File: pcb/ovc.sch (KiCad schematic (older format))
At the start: 234 parts

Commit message: finished schematic and starting location of components, advance in analog front end
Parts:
- removed C? (x21): C, symbol Device:C
- removed J? (x5): Conn_01x04, symbol Connector_Generic:Conn_01x04
- removed J? (x5): Conn_01x02, symbol Connector_Generic:Conn_01x02
- removed J?: Conn_02x03_Counter_Clockwise, symbol Connector_Generic:Conn_02x03_Counter_Clockwise
- removed R? (x2): R, VC:VC-RES-0603-1608metric, symbol Device:R
- removed R? (x2): 5k, VC:VC-RES-0603-1608metric, symbol Device:R
- removed R? (x6): 10k, VC:VC-RES-0603-1608metric, symbol Device:R
- added C14, C19, C2, C22, C24, C27, C28, C30, C32, C40, C41, C59, C6, C60, C62, C63, C70, C71, C73, C74, C80, C86: 100nF, VC:murata-CAP-GCM-0603-1608metric-reflow, symbol Device:C
- added C53, C78: 470uF, Capacitor_SMD:C_Elec_10x10.2, symbol Device:CP
- added C67, C79, C84, C85: 10uF, VC:murata-CAP-GRM-0805-2012metric-reflow, symbol Device:C
- added D12, D14: SM6T39CA, VC:ST-DO214AA, symbol vc_misc:SM6T39CA
- added D27: LTST-C191KRKT, digikey-footprints:LED_0603, symbol dk_LED-Indication-Discrete:LTST-C191KRKT
- added J1: Conn_01x12, VC:phoenix_contact-therminal_block-12pos_PTSA1.5_12-3.5-F-1985069, symbol Connector_Generic:Conn_01x12
- added J10, J11, J7, J8: Conn_01x04, Connector_Molex:Molex_Nano-Fit_105309-xx04_1x04_P2.50mm_Vertical, symbol Connector_Generic:Conn_01x04
- added J13: Conn_02x11_Odd_Even, Connector_PinHeader_2.54mm:PinHeader_2x11_P2.54mm_Vertical_SMD, symbol Connector_Generic:Conn_02x11_Odd_Even
- added J16: Conn_01x31, VC:Omron-XF2M-3015-1A, symbol Connector_Generic:Conn_01x31
- added J21, J22: Conn_01x08, Connector_PinHeader_2.54mm:PinHeader_1x08_P2.54mm_Vertical, symbol Connector_Generic:Conn_01x08
- added J23: Conn_01x10, Connector_FFC-FPC:Hirose_FH12-10S-0.5SH_1x10-1MP_P0.50mm_Horizontal, symbol Connector_Generic:Conn_01x10
- added J3: Conn_02x04_Counter_Clockwise, VC:VC-SOICbite-vcpinout, symbol Connector_Generic:Conn_02x04_Counter_Clockwise
- added J4: Conn_01x04, Connector_Phoenix_MSTB:PhoenixContact_MSTBA_2,5_4-G_1x04_P5.00mm_Horizontal, symbol Connector_Generic:Conn_01x04
- added J9: Conn_01x02, Connector_Phoenix_MSTB:PhoenixContact_MSTBA_2,5_2-G_1x02_P5.00mm_Horizontal, symbol Connector_Generic:Conn_01x02
- added Q10, Q11, Q12, Q8, Q9: MMBT3906, Package_TO_SOT_SMD:SOT-23, symbol Transistor_BJT:MMBT3906
- added R2, R4: 4.99k, VC:VC-RES-0603-1608metric, symbol Device:R
- added R29, R30: 10r, VC:VC-RES-0603-1608metric, symbol Device:R
- added R35, R36, R37: 5K1, VC:VC-RES-0603-1608metric, symbol Device:R
- added R63, R67, R75, R78, R81: 1k, VC:VC-RES-0603-1608metric, symbol Device:R
- added R69, R70, R71, R89, R90: 10k, VC:VC-RES-0603-1608metric, symbol Device:R
- added R83, R84, R85, R88, R91, R92, R93, R94, R95: 330, VC:VC-RES-0603-1608metric, symbol Device:R
- added U13, U15: SN74HC595N, digikey-footprints:DIP-16_W7.62mm, symbol dk_Logic-Shift-Registers:SN74HC595N
- added U7: SN74LVC3G17, VC:TexasInstruments_DCU8_R-PDSO-G8_0.5mm, symbol vc_misc:SN74LVC3G17
- C1, C11, C12, C16, C17, C18, C20, C21, C3, C31, C33, C34, C37, C38, C39, C43, C44, C46, C47, C48, C5, C56, C58, C7, C76, C81: renamed from C?; footprint (none) -> VC:murata-CAP-GCM-0603-1608metric-reflow
- C10, C50, C52, C68: renamed from C?; value C -> 100nF; footprint (none) -> VC:murata-CAP-GCM-0603-1608metric-reflow
- C13, C35, C36, C4, C45, C55, C57, C66, C83, C9: renamed from C?; footprint (none) -> VC:murata-CAP-GRM-0805-2012metric-reflow
- C42, C51, C61, C64, C69, C72, C75: renamed from C?; value CP -> 47uF; footprint (none) -> Capacitor_SMD:C_Elec_6.3x5.8
- C54: renamed from C?; value CP -> 470uF; footprint (none) -> Capacitor_SMD:C_Elec_10x10.2
- J12: renamed from J?; footprint (none) -> Connector_PinHeader_2.54mm:PinHeader_2x10_P2.54mm_Vertical_SMD
- J14, J15: renamed from J?; footprint (none) -> Connector_PinHeader_2.54mm:PinHeader_1x04_P2.54mm_Vertical
- J18: renamed from J?; footprint (none) -> Connector_PinHeader_2.54mm:PinHeader_1x13_P2.54mm_Vertical_SMD_Pin1Left
- J19: renamed from J?; footprint (none) -> Connector_PinHeader_2.54mm:PinHeader_1x14_P2.54mm_Vertical_SMD_Pin1Left
- J2: renamed from J?; footprint (none) -> Connector_Card:microSD_HC_Hirose_DM3AT-SF-PEJM5
- J20: renamed from J?; footprint (none) -> Connector_PinHeader_1.27mm:PinHeader_1x06_P1.27mm_Vertical_SMD_Pin1Left
- J5: renamed from J?; footprint (none) -> Connector_Molex:Molex_Nano-Fit_105309-xx04_1x04_P2.50mm_Vertical
- J6: renamed from J?; footprint (none) -> Connector_PinHeader_2.54mm:PinHeader_1x02_P2.54mm_Vertical
- JP1: renamed from JP?; footprint (none) -> Connector_PinHeader_2.00mm:PinHeader_1x03_P2.00mm_Vertical
- R52, R61: renamed from R?; footprint VC:VC-RES-0603-1608metric -> digikey-footprints:1206
- gave numbers to parts that had none: 132
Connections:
- net +12V: now also C41.1, C53.1, C60.1, C63.1, C71.1, C74.1, J9.1 (Pin_1)
- net +24V: now also C78.1, J1.6 (Pin_6), J1.8 (Pin_8)
- net +3.3VA: now also R35.1, R36.1, R37.1
- net +3V3: now also J12.1 (Pin_1), J12.17 (Pin_17), J12.18 (Pin_18), J12.2 (Pin_2), C14.1, C19.1, C2.1, C22.1, C24.1, C27.1, C28.1, C30.1, C40.1, C59.1, C6.1, C62.1, C70.1, C73.1, J13.2 (Pin_2), J3.8 (Pin_8)
- net +5V: now also J12.16 (Pin_16), C32.1, C67.1, C79.1, C80.1, C84.1, C85.1, C86.1, J16.26 (Pin_26), J16.27 (Pin_27), J23.10 (Pin_10), J23.9 (Pin_9), Q10.2 (E), Q11.2 (E), Q12.2 (E), Q8.2 (E), Q9.2 (E), R71.1, R90.1, U13.16 (VCC), U15.16 (VCC), U7.8 (VCC)
- net CJ-ALERT: now also R35.2
- net CJ-SCL: now also R36.2
- net CJ-SDA: now also R37.2
- net CLKI: now also U4.49 (RC12/OSC1/CLKI)
- net GND: now also J12.19 (Pin_19), J12.20 (Pin_20), J12.7 (Pin_7), J12.8 (Pin_8), C14.2, C19.2, C2.2, C22.2, C24.2, C27.2, C28.2, C30.2, C32.2, C40.2, C41.2, C53.2, C59.2, C6.2, C60.2, C62.2, C63.2, C67.2, C70.2, C71.2, C73.2, C74.2, C78.2, C79.2, C80.2, C84.2, C85.2, C86.2, D12.2, D14.2, D27.1, J13.4 (Pin_4), J13.6 (Pin_6), J16.1 (Pin_1), J16.21 (Pin_21), J16.25 (Pin_25), J16.30 (Pin_30), J16.31 (Pin_31), J23.1 (Pin_1), J23.2 (Pin_2), J23.7 (Pin_7), J3.5 (Pin_5), J4.2 (Pin_2), J4.4 (Pin_4), J9.2 (Pin_2), R4.2, R69.2, R70.2, R89.2, U13.8 (GND), U15.8 (GND), U7.4 (GND), U7.6 (3A)
- net LED3: now also U13.15 (QA); no longer U4.28 (RA9/AN27/VREF-/CVREF-/AERXD2)
- net LED4: now also U13.1 (QB); no longer U4.29 (RA10/AN28/VREF+/CVREF+/AERXD3)
- net MCLR: now also J3.1 (Pin_1)
- net PGEC1: now also J12.3 (Pin_3), J3.2 (Pin_2)
- net PGED1: now also J12.4 (Pin_4), J3.3 (Pin_3)
- net SCL2: now also J12.11 (Pin_11)
- net SCL3: no longer U4.58 (RF8/SCL3/RPF8/EBIRDY2)
- net SDA2: now also J12.13 (Pin_13)
- net SDA3: now also J12.10 (Pin_10)
- net SW3: now also U4.23 (RB2/AN2/RPB2/C2INB); no longer U4.22 (RB3/AN3/RPB3/C2INA)
- net SW4: now also U4.32 (RB8/AN48/PMA10/RPB8/EBIA10); no longer U4.23 (RB2/AN2/RPB2/C2INB)
- net W-RX: now also U4.48 (RD15/AN33/SCK6/RPD15/AETXD1); no longer U4.44 (RB15/AN10/PMA0/OCFB/RPB15/AETXD2/ERXD3/EBIA0)
- net W-TX: now also U4.47 (RD14/AN32/RPD14/AETXD0); no longer U4.43 (RB14/AN9/PMA1/SCK3/RPB14/AETXD3/ERXD2/EBIA1)
- net TH2-I1: now reaches C65.1, D19.1, R44.2, U10.2 (BIAS)
- net TH2-I1: now also J1.2 (Pin_2)
- net at C11.1, C7.1, U3.5 (REFP0/GPIO0): now also R2.1
- net at C11.2, C12.2, U3.6 (REFN0/GPIO0): now also R4.1
- net at C8.1, D1.1, R3.1: now also J1.12 (Pin_12), R2.2
- net at C15.1, D2.1, R8.2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: now also J1.11 (Pin_11)
- net at C23.1, D3.1, R12.2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: now also J1.10 (Pin_10)
- net at C25.1, D4.K, D5.1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: now also J1.9 (Pin_9)
- net TH1-I1: now reaches C33.1, C35.1, D10.1, R27.2
- net TH1-I1: now also J1.4 (Pin_4)
- net TH1-I2: now reaches C35.2, C37.2, D15.1, R31.2, R32.2, R34.1
- net TH1-I2: now also J1.3 (Pin_3)
- net TH2-I2: now reaches C49.1, D18.1, R43.2
- net TH2-I2: now also J1.1 (Pin_1)
- net CIN-1: now reaches R50.2
- net CIN-1: now also J1.7 (Pin_7)
- net CIN-2: now reaches R56.2
- net CIN-2: now also J1.5 (Pin_5)
- net RF12: now reaches U4.40 (RF12/AN31/RPF12/EBIA17/TDO)
- net RF12: now also J12.5 (Pin_5)
- net DS-BT: now reaches U4.50 (RC15/OSC2/CLKO)
- net DS-BT: now also R69.1, U13.12 (RCLK), U15.12 (RCLK)
- net MCUTX-F3: now reaches U4.56 (RF3/USBID/RPF3)
- net MCUTX-F3: now also J12.9 (Pin_9), J16.23 (Pin_23), J23.5 (Pin_5)
- net 4DRST-A4: now reaches U4.61 (RA4/PMA14/PMCS1/EBIA14)
- net 4DRST-A4: now also J12.14 (Pin_14), J16.22 (Pin_22), J23.3 (Pin_3)
- net RE0: now reaches U4.91 (RE0/PMD0/EBID0)
- net RE0: now also J12.15 (Pin_15)
- net at A3.3 (M1B): now also J8.1 (Pin_1)
- net at A3.4 (M1A): now also J8.2 (Pin_2)
- net at A3.5 (M2A): now also J8.3 (Pin_3)
- net at A3.6 (M2B): now also J8.4 (Pin_4)
- net at A5.3 (M1B): now also J11.1 (Pin_1)
- net at A5.4 (M1A): now also J11.2 (Pin_2)
- net at A5.5 (M2A): now also J11.3 (Pin_3)
- net at A5.6 (M2B): now also J11.4 (Pin_4)
- net at A4.3 (M1B): now also J10.1 (Pin_1)
- net at A4.4 (M1A): now also J10.2 (Pin_2)
- net at A4.5 (M2A): now also J10.3 (Pin_3)
- net at A4.6 (M2B): now also J10.4 (Pin_4)
- net at A2.3 (M1B): now also J7.1 (Pin_1)
- net at A2.4 (M1A): now also J7.2 (Pin_2)
- net at A2.5 (M2A): now also J7.3 (Pin_3)
- net at A2.6 (M2B): now also J7.4 (Pin_4)
- net MCURX-SCL3: now reaches J12.12 (Pin_12)
- net MCURX-SCL3: now also U4.58 (RF8/SCL3/RPF8/EBIRDY2), J16.24 (Pin_24), J23.6 (Pin_6)
- net RB15: now reaches J12.6 (Pin_6)
- net RB15: now also U4.44 (RB15/AN10/PMA0/OCFB/RPB15/AETXD2/ERXD3/EBIA0)
- new net: R71.2, U13.10 (~SRCLR)
- new net: R70.1, U13.13 (~OE)
- new net: R63.2, U13.3 (QD)
- new net: R67.2, U13.4 (QE)
- new net: R75.2, U13.5 (QF)
- new net: R78.2, U13.6 (QG)
- new net: R81.2, U13.7 (QH)
- new net: U13.9 (QH'), U15.14 (SER)
- new net: R85.2, U15.1 (QB)
- new net: R90.2, U15.10 (~SRCLR)
- new net: R89.1, U15.13 (~OE)
- new net: R84.2, U15.15 (QA)
- new net: R88.2, U15.2 (QC)
- new net: R91.2, U15.3 (QD)
- new net: R92.2, U15.4 (QE)
- new net: R93.2, U15.5 (QF)
- new net: R94.2, U15.6 (QG)
- new net: R95.2, U15.7 (QH)
- new net: J13.17 (Pin_17), J16.10 (Pin_10)
- new net: J13.19 (Pin_19), J16.11 (Pin_11)
- new net: J13.21 (Pin_21), J16.12 (Pin_12)
- new net: J13.22 (Pin_22), J16.13 (Pin_13)
- new net: J13.20 (Pin_20), J16.14 (Pin_14)
- new net: J13.18 (Pin_18), J16.15 (Pin_15)
- new net: J13.16 (Pin_16), J16.16 (Pin_16)
- new net: J13.14 (Pin_14), J16.17 (Pin_17)
- new net: J13.12 (Pin_12), J16.18 (Pin_18)
- new net: J13.10 (Pin_10), J16.19 (Pin_19)
- new net: J13.1 (Pin_1), J16.2 (Pin_2)
- new net: J13.8 (Pin_8), J16.20 (Pin_20)
- new net: J13.3 (Pin_3), J16.3 (Pin_3)
- new net: J13.5 (Pin_5), J16.4 (Pin_4)
- new net: J13.7 (Pin_7), J16.5 (Pin_5)
- new net: J13.9 (Pin_9), J16.6 (Pin_6)
- new net: J13.11 (Pin_11), J16.7 (Pin_7)
- new net: J13.13 (Pin_13), J16.8 (Pin_8)
- new net: J13.15 (Pin_15), J16.9 (Pin_9)
- new net: Q11.1 (B), R67.1
- new net: Q8.1 (B), R63.1
- new net: Q9.1 (B), R75.1
- new net: Q12.1 (B), R78.1
- new net: Q10.1 (B), R81.1
- new net: R30.2, U7.5 (2Y)
- new net: R29.2, U7.7 (1Y)
- new net: D12.1, J4.1 (Pin_1), R29.1
- new net: D14.1, J4.3 (Pin_3), R30.1
- new net: D27.2, R83.2
- new net A,L1: J22.6 (Pin_6), R88.1
- new net B,L2: J22.8 (Pin_8), R84.1
- new net C,L3: J22.5 (Pin_5), R91.1
- new net CA-1: J21.1 (Pin_1), Q10.3 (C)
- new net CA-2: J21.2 (Pin_2), Q12.3 (C)
- new net CA-3: J21.6 (Pin_6), Q11.3 (C)
- new net CA-4: J21.8 (Pin_8), Q8.3 (C)
- new net CA-L: J21.4 (Pin_4), Q9.3 (C)
- new net D: J21.3 (Pin_3), R95.1
- new net DP: J21.7 (Pin_7), R93.1
- new net DS-SCLK: U13.11 (SRCLK), U15.11 (SRCLK), U4.43 (RB14/AN9/PMA1/SCK3/RPB14/AETXD3/ERXD2/EBIA1)
- new net DS-SD: U13.14 (SER), U4.22 (RB3/AN3/RPB3/C2INA)
- new net E: J21.5 (Pin_5), R94.1
- new net F: J22.3 (Pin_3), R92.1
- new net G: J22.7 (Pin_7), R85.1
- new net LED5: R83.1, U13.2 (QC)
- new net SSR-1: U4.28 (RA9/AN27/VREF-/CVREF-/AERXD2), U7.1 (1A)
- new net SSR-2: U4.29 (RA10/AN28/VREF+/CVREF+/AERXD3), U7.3 (2A)
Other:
- note added: "Order extendended temperature version"
- note added: "Place both connectors close to each other"
- note removed: "Order extendentemperature version"
- note removed: "agregar:\n- headers\n- puertos para display: \n *O128O064DGPP3N0000\n *4Dsystems\n\n"
- moved on the sheet: A1, A2, A3, A4, A5, C1, C10, C11, C12, C13, C15, C16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

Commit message: finished schematic, layed out components in pcb and advanced in routing
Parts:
- removed C51: 47uF, Capacitor_SMD:C_Elec_6.3x5.8, symbol Device:CP
- removed J1: Conn_01x12, VC:phoenix_contact-therminal_block-12pos_PTSA1.5_12-3.5-F-1985069, symbol Connector_Generic:Conn_01x12
- removed J14, J15: Conn_01x04, Connector_PinHeader_2.54mm:PinHeader_1x04_P2.54mm_Vertical, symbol Connector_Generic:Conn_01x04
- removed J18: Conn_01x13, Connector_PinHeader_2.54mm:PinHeader_1x13_P2.54mm_Vertical_SMD_Pin1Left, symbol Connector_Generic:Conn_01x13
- removed J19: Conn_01x14, Connector_PinHeader_2.54mm:PinHeader_1x14_P2.54mm_Vertical_SMD_Pin1Left, symbol Connector_Generic:Conn_01x14
- removed J21, J22: Conn_01x08, Connector_PinHeader_2.54mm:PinHeader_1x08_P2.54mm_Vertical, symbol Connector_Generic:Conn_01x08
- removed J9: Conn_01x02, Connector_Phoenix_MSTB:PhoenixContact_MSTBA_2,5_2-G_1x02_P5.00mm_Horizontal, symbol Connector_Generic:Conn_01x02
- added C51, C87: 10uF, VC:murata-CAP-GRM-0805-2012metric-reflow, symbol Device:C
- added D28: MBR2H200SFT3G, VC:onsemi-sod123fl, symbol vc_diode_rectifier:MBR2H200SFT3G
- added D29: LTST-C191KRKT, digikey-footprints:LED_0603, symbol dk_LED-Indication-Discrete:LTST-C191KRKT
- added DS1: LTC-4627JF, VC:liteon-C4627JF, symbol vc_misc:LTC-4627JF
- added J1: Conn_01x13, VC:phoenix_contact-therminal_block-13pos_PTSA1.5_13-3.5-F-1985072, symbol Connector_Generic:Conn_01x13
- added J14: Conn_02x18_Odd_Even, Connector_PinHeader_2.54mm:PinHeader_2x18_P2.54mm_Vertical_SMD, symbol Connector_Generic:Conn_02x18_Odd_Even
- added J15: Conn_01x02, VC:phoenix_contact-therminal_block-2pos_PTSA1.5-2-3.5-F-1984963, symbol Connector_Generic:Conn_01x02
- added J18: Conn_02x03_Odd_Even, Connector_PinHeader_2.54mm:PinHeader_2x03_P2.54mm_Vertical, symbol Connector_Generic:Conn_02x03_Odd_Even
- added J9: Conn_01x04, VC:phoenix_contact-therminal_block-4pos_PTSA1.5-4-3.5-F-1984989, symbol Connector_Generic:Conn_01x04
- added Q13: FDV301N, digikey-footprints:SOT-23-3, symbol dk_Transistors-FETs-MOSFETs-Single:FDV301N
- added R96: 10k, VC:VC-RES-0603-1608metric, symbol Device:R
- added R97: 330, VC:VC-RES-0603-1608metric, symbol Device:R
- added RLY3: G6DN-1A-L_DC5, VC:Omron G6DN-1A, symbol vc_misc:G6DN-1A-L_DC5
- C50: value 100nF -> 10uF; footprint VC:murata-CAP-GCM-0603-1608metric-reflow -> VC:murata-CAP-GRM-0805-2012metric-reflow
- J13: footprint Connector_PinHeader_2.54mm:PinHeader_2x11_P2.54mm_Vertical_SMD -> Connector_PinHeader_2.54mm:PinHeader_2x12_P2.54mm_Vertical_SMD
- J4: footprint Connector_Phoenix_MSTB:PhoenixContact_MSTBA_2,5_4-G_1x04_P5.00mm_Horizontal -> VC:phoenix_contact-therminal_block-4pos_PTSA1.5-4-3.5-F-1984989
- U13, U15: footprint digikey-footprints:DIP-16_W7.62mm -> digikey-footprints:SOIC-16_W3.90mm
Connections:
- net SCL3 is gone; now on net MCURX-SCL3: R25.2, R26.2
- net +12V: now also J9.1 (Pin_1), J9.2 (Pin_2)
- net +24V: now also J1.7 (Pin_7), J1.9 (Pin_9)
- net +3.3VA: now also J18.3 (Pin_3)
- net +3V3: now also J14.1 (Pin_1), J14.2 (Pin_2), J14.3 (Pin_3), J14.4 (Pin_4), J18.1 (Pin_1); no longer C6.1, U2.8 (VCC)
- net +5V: now also C6.1, J12.15 (Pin_15), U2.8 (VCC), C51.1, C87.1, D28.K, J18.5 (Pin_5), R97.1, RLY3.1 (C1)
- net A,L1: now also DS1.14 (A/L1)
- net B,L2: now also DS1.16 (B/L2)
- net BRDN1_N: now also C81.2, R65.1, U3.16 (AIN7/IEXC/GPIO7); no longer C76.2, R53.1, U3.14 (AIN5/IEXC/GPIO5)
- net BRDN2_N: now also C76.2, R53.1, U3.14 (AIN5/IEXC/GPIO5); no longer C81.2, R65.1, U3.16 (AIN7/IEXC/GPIO7)
- net C,L3: now also DS1.13 (C/L3)
- net CA-1: now also Q8.3 (C), DS1.1 (CA-D1); no longer Q10.3 (C)
- net CA-2: now also Q11.3 (C), DS1.2 (CA-D2); no longer Q12.3 (C)
- net CA-3: now also Q12.3 (C), DS1.6 (CA-D3); no longer Q11.3 (C)
- net CA-4: now also Q10.3 (C), DS1.8 (CA-D4); no longer Q8.3 (C)
- net CA-L: now also DS1.4 (CA-L1,L2,L3)
- net CIN-1: now also J1.6 (Pin_6)
- net CIN-2: now also J1.8 (Pin_8)
- net CLKI: no longer U4.20 (RB5/AN45/RPB5/C1INA)
- net D: now also R93.1, DS1.3 (D); no longer R95.1
- net D+: now also D17.3; no longer D17.1
- net D-: now also D17.1; no longer D17.3
- net DD+: now also D17.4; no longer D17.6
- net DD-: now also D17.6; no longer D17.4
- net DP: now also R95.1, DS1.7 (DP); no longer R93.1
- net E: now also DS1.5 (E)
- net F: now also DS1.11 (F)
- net G: now also DS1.15 (G)
- net GND: now also C51.2, C87.2, J1.5 (Pin_5), J14.5 (Pin_5), J14.6 (Pin_6), J14.7 (Pin_7), J14.8 (Pin_8), J14.9 (Pin_9), J18.2 (Pin_2), J18.4 (Pin_4), J18.6 (Pin_6), J9.3 (Pin_3), J9.4 (Pin_4), Q13.2 (S)
- net RE0: now also R96.2; no longer J12.15 (Pin_15)
- net THERM_N: now also C34.1, C36.1, R28.1, U3.17 (AIN2/IEXC/GPIO2); no longer C36.2, C38.2, R33.1, U3.18 (AIN3/IEXC/GPIO3)
- net THERM_P: now also C36.2, C38.2, R33.1, U3.18 (AIN3/IEXC/GPIO3); no longer C34.1, C36.1, R28.1, U3.17 (AIN2/IEXC/GPIO2)
- net W-BOOT: now also J14.32 (Pin_32)
- net W-CTS: now also J14.36 (Pin_36)
- net W-IO1: now also J14.14 (Pin_14)
- net W-IO18: now also J14.22 (Pin_22)
- net W-IO19: now also J14.20 (Pin_20)
- net W-IO2: now also J14.34 (Pin_34)
- net W-IO21: now also J14.18 (Pin_18)
- net W-IO22: now also J14.12 (Pin_12)
- net W-IO23: now also J14.10 (Pin_10)
- net W-IO25: now also J14.25 (Pin_25)
- net W-IO26: now also J14.27 (Pin_27)
- net W-IO27: now also J14.29 (Pin_29)
- net W-IO3: now also J14.16 (Pin_16)
- net W-IO32: now also J14.21 (Pin_21)
- net W-IO33: now also J14.23 (Pin_23)
- net W-IO34: now also J14.17 (Pin_17)
- net W-IO35: now also J14.19 (Pin_19)
- net W-IO4: now also J14.30 (Pin_30)
- net W-IO5: now also J14.24 (Pin_24)
- net W-RTS: now also J14.31 (Pin_31)
- net W-RX: now also J14.28 (Pin_28)
- net W-RX0: now also J14.35 (Pin_35)
- net W-SVN: now also J14.15 (Pin_15)
- net W-SVP: now also J14.13 (Pin_13)
- net W-TX: now also J14.26 (Pin_26)
- net W-TX0: now also J14.33 (Pin_33)
- net W_EN: now also J14.11 (Pin_11)
- net at C8.1, D1.1, R2.2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: now also J1.13 (Pin_13)
- net at Q6.1 (S), Q6.2 (S), Q6.3 (S): now also R57.2, R61.1; no longer R51.2, R52.1
- net at C15.1, D2.1, R8.2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: now also J1.12 (Pin_12)
- net at C23.1, D3.1, R12.2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: now also J1.11 (Pin_11)
- net at C25.1, D4.K, D5.1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: now also J1.10 (Pin_10)
- net at R61.2, R65.2: now also D21.2 (A); no longer D21.1 (A)
- net at R52.2, R53.2: now also D21.1 (A); no longer D21.2 (A)
- net THPF_N: now reaches D11.K, D9.A, R27.1, R28.2
- net THPF_P: now reaches D13.A, D16.K, R32.1, R33.2
- net at Q7.1 (S), Q7.2 (S), Q7.3 (S): now also R51.2, R52.1; no longer R57.2, R61.1
- net BRD1_P renamed BRDN2_P
- net BRD2_P renamed BRDN1_P
- net TH1-I1 renamed TH1_N
- net TH1_N: now also R31.2, R34.1, J1.4 (Pin_4)
- net TH1-I2 renamed TH1_P
- net TH1_P: now also J1.3 (Pin_3); no longer R31.2, R34.1
- net TH2-I1 renamed TH2-N
- net TH2-N: now also J1.2 (Pin_2)
- net TH2-I2 renamed TH2-P
- net TH2-P: now also J1.1 (Pin_1)
- new net: D28.A, D29.1, Q13.3 (D), RLY3.2 (C2)
- new net: D29.2, R97.2
- new net: Q13.1 (G), R96.1
- new net: J15.2 (Pin_2), RLY3.3 (A)
- new net: J15.1 (Pin_1), RLY3.4 (B)
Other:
- note added: "GET A HIGH PRECISION LOW DRIFT RESISTOR"
- moved on the sheet: C47, C76, C81, C83, D17, J17, R31, R34, R51, R52, R53, R57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

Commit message: gerber generated and fabricated
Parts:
- removed J1: Conn_01x13, VC:phoenix_contact-therminal_block-13pos_PTSA1.5_13-3.5-F-1985072, symbol Connector_Generic:Conn_01x13
- removed J4: Conn_01x04, VC:phoenix_contact-therminal_block-4pos_PTSA1.5-4-3.5-F-1984989, symbol Connector_Generic:Conn_01x04
- added C88, C89: 10uF, VC:murata-CAP-GRM-0805-2012metric-reflow, symbol Device:C
- added J1: Conn_01x16, VC:phoenix_contact-therminal_block-16pos_PTSA1.5_16-3.5-F-1985108, symbol Connector_Generic:Conn_01x16
- J20: footprint Connector_PinHeader_1.27mm:PinHeader_1x06_P1.27mm_Vertical_SMD_Pin1Left -> Connector_PinHeader_1.27mm:PinHeader_1x06_P1.27mm_Vertical_SMD_Pin1Right
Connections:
- net +24V: now also J1.10 (Pin_10), J1.12 (Pin_12)
- net +3.3VA: no longer J18.3 (Pin_3), R62.1, R74.1, R80.1, R86.1
- net +3V3: now also J18.3 (Pin_3), R62.1, R74.1, R80.1, R86.1, C88.1, C89.1
- net CIN-1: now also J1.9 (Pin_9)
- net CIN-2: now also J1.11 (Pin_11)
- net GND: now also J14.10 (Pin_10), C88.2, C89.2, J1.3 (Pin_3), J1.8 (Pin_8); no longer J14.9 (Pin_9)
- net M1-CS: now also U4.66 (RA14/SCL1/RPA14/AETXCLK); no longer U4.68 (RD9/PMA15/PMCS2/RPD9/EBIA15)
- net M1-DIR: now also U4.64 (RF4/PMA9/SDA5/RPF4/EBIA9); no longer U4.66 (RA14/SCL1/RPA14/AETXCLK)
- net M1-EN: now also U4.68 (RD9/PMA15/PMCS2/RPD9/EBIA15); no longer U4.64 (RF4/PMA9/SDA5/RPF4/EBIA9)
- net M2-CS: now also U4.76 (RD1/SCK1/RPD1); no longer U4.73 (RC14/T1CK/RPC14/SOSCO)
- net M2-DIR: now also U4.71 (RD0/INT0/RTCC/RPD0/AEMDIO/EMDIO); no longer U4.77 (RD2/PMD14/RPD2/ETXEN/EBID14)
- net M2-EN: now also U4.77 (RD2/PMD14/RPD2/ETXEN/EBID14); no longer U4.71 (RD0/INT0/RTCC/RPD0/AEMDIO/EMDIO)
- net M2-STP: now also U4.73 (RC14/T1CK/RPC14/SOSCO); no longer U4.76 (RD1/SCK1/RPD1)
- net M4-CS: now also A4.12 (CS); no longer A5.12 (CS)
- net M4-DIR: now also A4.16 (DIR); no longer A5.16 (DIR)
- net M4-EN: now also A4.9 (EN); no longer A5.9 (EN)
- net M4-STP: now also A4.15 (STEP); no longer A5.15 (STEP)
- net M5-CS: now also A5.12 (CS), U4.99 (RE3/PMD3/RPE3/EBID3); no longer A4.12 (CS), U4.98 (RE2/PMD2/EBID2)
- net M5-DIR: now also A5.16 (DIR), U4.94 (RE1/PMD1/EBID1); no longer A4.16 (DIR), U4.99 (RE3/PMD3/RPE3/EBID3)
- net M5-EN: now also A5.9 (EN), U4.100 (RE4/PMD4/AN18/EBID4); no longer A4.9 (EN), U4.94 (RE1/PMD1/EBID1)
- net M5-STP: now also A5.15 (STEP), U4.98 (RE2/PMD2/EBID2); no longer A4.15 (STEP), U4.100 (RE4/PMD4/AN18/EBID4)
- net TH1_N: now also J1.7 (Pin_7)
- net TH1_P: now also J1.6 (Pin_6)
- net TH2-N: now also J1.5 (Pin_5)
- net TH2-P: now also J1.4 (Pin_4)
- net W-BOOT: now also J14.31 (Pin_31); no longer J14.32 (Pin_32)
- net W-CTS: now also J14.35 (Pin_35); no longer J14.36 (Pin_36)
- net W-IO1: now also J14.13 (Pin_13); no longer J14.14 (Pin_14)
- net W-IO18: now also J14.21 (Pin_21); no longer J14.22 (Pin_22)
- net W-IO19: now also J14.19 (Pin_19); no longer J14.20 (Pin_20)
- net W-IO2: now also J14.33 (Pin_33); no longer J14.34 (Pin_34)
- net W-IO21: now also J14.17 (Pin_17); no longer J14.18 (Pin_18)
- net W-IO22: now also J14.11 (Pin_11); no longer J14.12 (Pin_12)
- net W-IO23: now also J14.9 (Pin_9); no longer J14.10 (Pin_10)
- net W-IO25: now also J14.26 (Pin_26); no longer J14.25 (Pin_25)
- net W-IO26: now also J14.28 (Pin_28); no longer J14.27 (Pin_27)
- net W-IO27: now also J14.30 (Pin_30); no longer J14.29 (Pin_29)
- net W-IO3: now also J14.15 (Pin_15); no longer J14.16 (Pin_16)
- net W-IO32: now also J14.22 (Pin_22); no longer J14.21 (Pin_21)
- net W-IO33: now also J14.24 (Pin_24); no longer J14.23 (Pin_23)
- net W-IO34: now also J14.18 (Pin_18); no longer J14.17 (Pin_17)
- net W-IO35: now also J14.20 (Pin_20); no longer J14.19 (Pin_19)
- net W-IO4: now also J14.29 (Pin_29); no longer J14.30 (Pin_30)
- net W-IO5: now also J14.23 (Pin_23); no longer J14.24 (Pin_24)
- net W-RTS: now also J14.32 (Pin_32); no longer J14.31 (Pin_31)
- net W-RX: now also J14.27 (Pin_27); no longer J14.28 (Pin_28)
- net W-RX0: now also J14.36 (Pin_36); no longer J14.35 (Pin_35)
- net W-SVN: now also J14.16 (Pin_16); no longer J14.15 (Pin_15)
- net W-SVP: now also J14.14 (Pin_14); no longer J14.13 (Pin_13)
- net W-TX: now also J14.25 (Pin_25); no longer J14.26 (Pin_26)
- net W-TX0: now also J14.34 (Pin_34); no longer J14.33 (Pin_33)
- net W_EN: now also J14.12 (Pin_12); no longer J14.11 (Pin_11)
- net at C8.1, D1.1, R2.2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: now also J1.16 (Pin_16)
- net at C15.1, D2.1, R8.2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: now also J1.15 (Pin_15)
- net at C23.1, D3.1, R12.2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: now also J1.14 (Pin_14)
- net at C25.1, D4.K, D5.1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: now also J1.13 (Pin_13)
- net at J16.13 (Pin_13): now also J13.12 (Pin_12); no longer J13.22 (Pin_22)
- net at J16.14 (Pin_14): now also J13.10 (Pin_10); no longer J13.20 (Pin_20)
- net at J16.15 (Pin_15): now also J13.8 (Pin_8); no longer J13.18 (Pin_18)
- net at J16.18 (Pin_18): now also J13.18 (Pin_18); no longer J13.12 (Pin_12)
- net at J16.19 (Pin_19): now also J13.20 (Pin_20); no longer J13.10 (Pin_10)
- net at J16.20 (Pin_20): now also J13.22 (Pin_22); no longer J13.8 (Pin_8)
- net SSRD-1: now reaches D12.1, R29.1
- net SSRD-1: now also J1.1 (Pin_1)
- net SSRD-2: now reaches D14.1, R30.1
- net SSRD-2: now also J1.2 (Pin_2)
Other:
- note added: "Se modificó paquete de libreria de Digikey\n en base a formato sugerido en hoja de datos"
- moved on the sheet: C32, D12, D14, R29, R30, U7

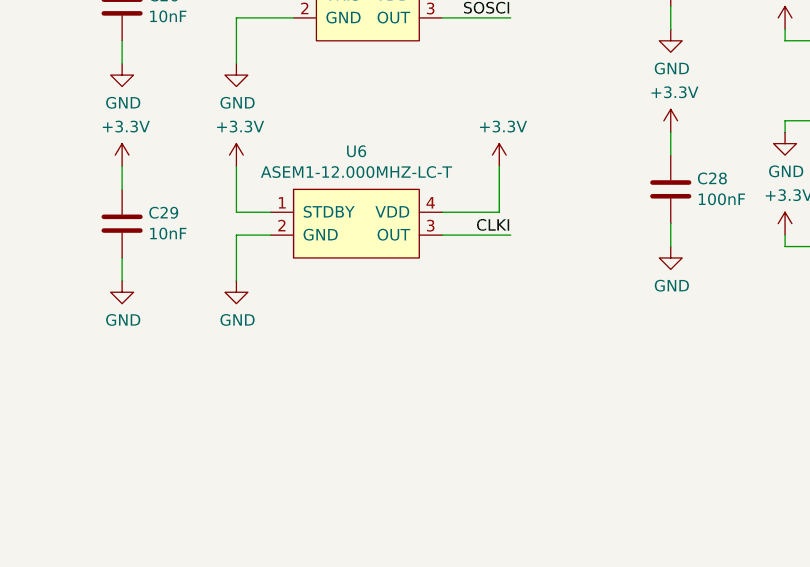
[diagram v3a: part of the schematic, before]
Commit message: Started module testing firmware
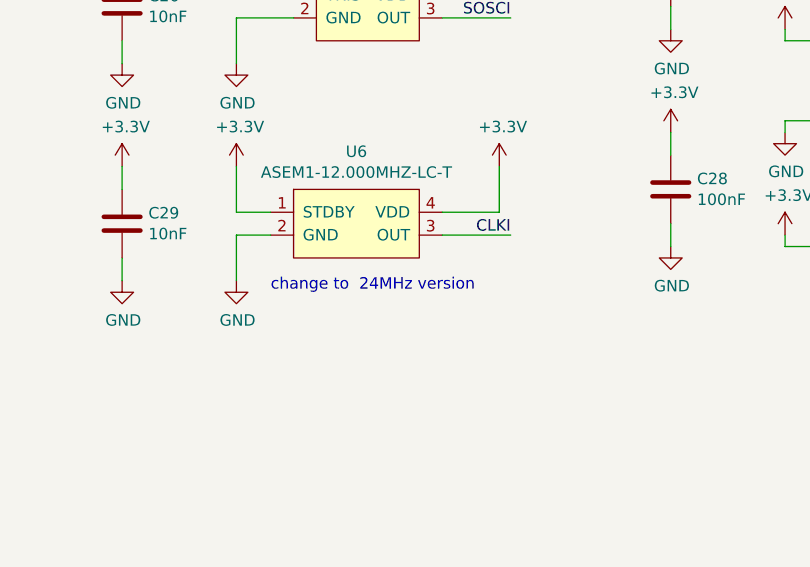
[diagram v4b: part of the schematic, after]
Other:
- note added: "change to 24MHz version"
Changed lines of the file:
@@
 Text Label 1350 2950 2    50   ~ 0
 SSRD-2
+Text Notes 14500 5750 0    50   ~ 0
+change to  24MHz version
 $EndSCHEMATC

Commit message: advances in firmware
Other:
- note added: "ANALOG FRONTEND"
- note added: "CONTROL OUTPUTS"
- note added: "DISPLAY AND USER INPUT"
- note added: "POWER REGULATION AND USB"
- note added: "TMC2130 STEPPER MOTOR DRIVER SOCKETS"
- note added: "WIRELESS"
- moved on the sheet: A1, A2, A3, A4, A5, C1, C10, C14, C16, C19, C2, C21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
